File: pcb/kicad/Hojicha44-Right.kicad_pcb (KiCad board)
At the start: 2 copper layers, 150.5 x 114.6 mm, 54 parts

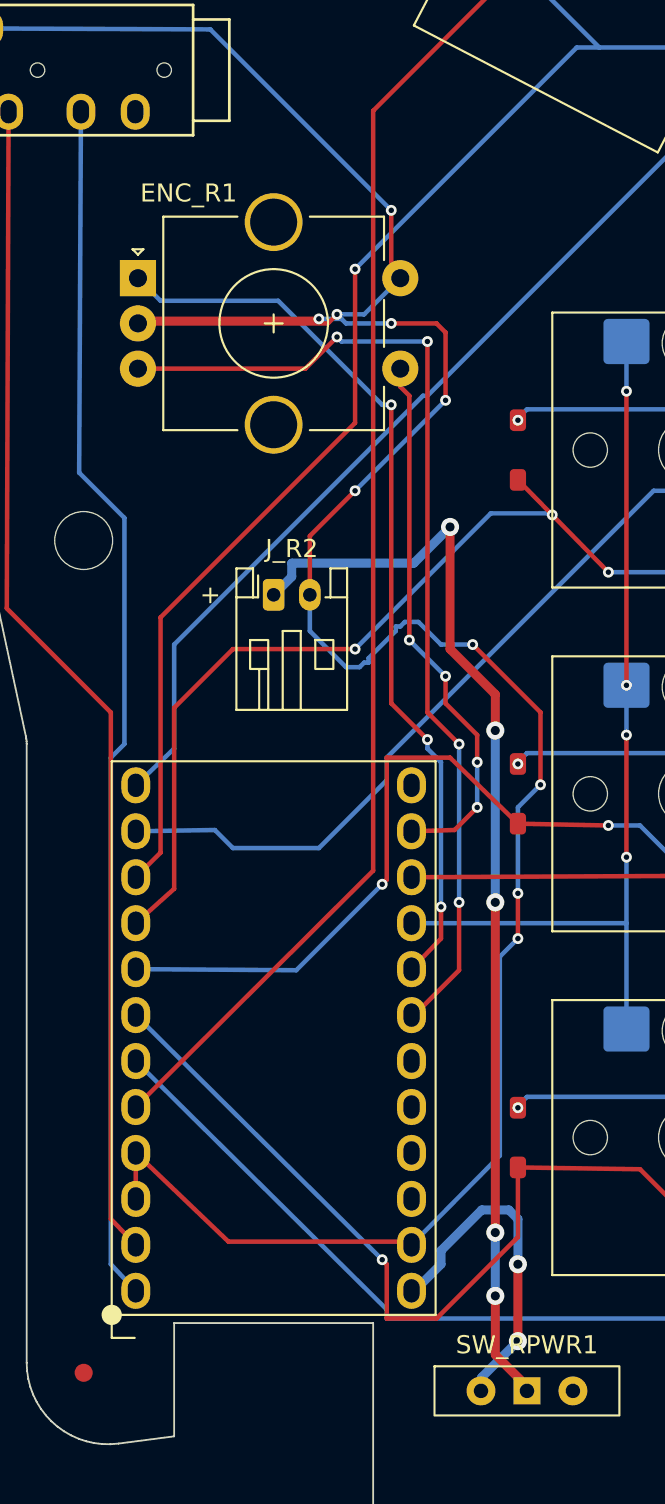
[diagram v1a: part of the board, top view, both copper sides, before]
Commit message: VBAT off USB notch + mask expansion + rating corrections
- Router r13: power-class notch keepout (bite band floor-0.5 to
  floor+2) moves the battery rail off the plug-bump edge; measured
  min VBAT copper-edge to outline 2.518mm both halves (was 0.25mm
  at the notch floor with a via at (111.75,47.5) — both gone).
- Carve/re-block: other-net clearance re-blocked after own carve so
  shared THT slivers steer exits instead of grazing (fixed the
  GND-vs-COL2 graze the reroute exposed). DRC green both halves.
- Mask expansion 0.05 (was 0) in both .kicad_pro; no reroute needed.
- WS-SLTV corrected to 300mA switching; boost jumper stays OPEN;
  100x100 pricing note; USB-cable dry-fit note in first-article.
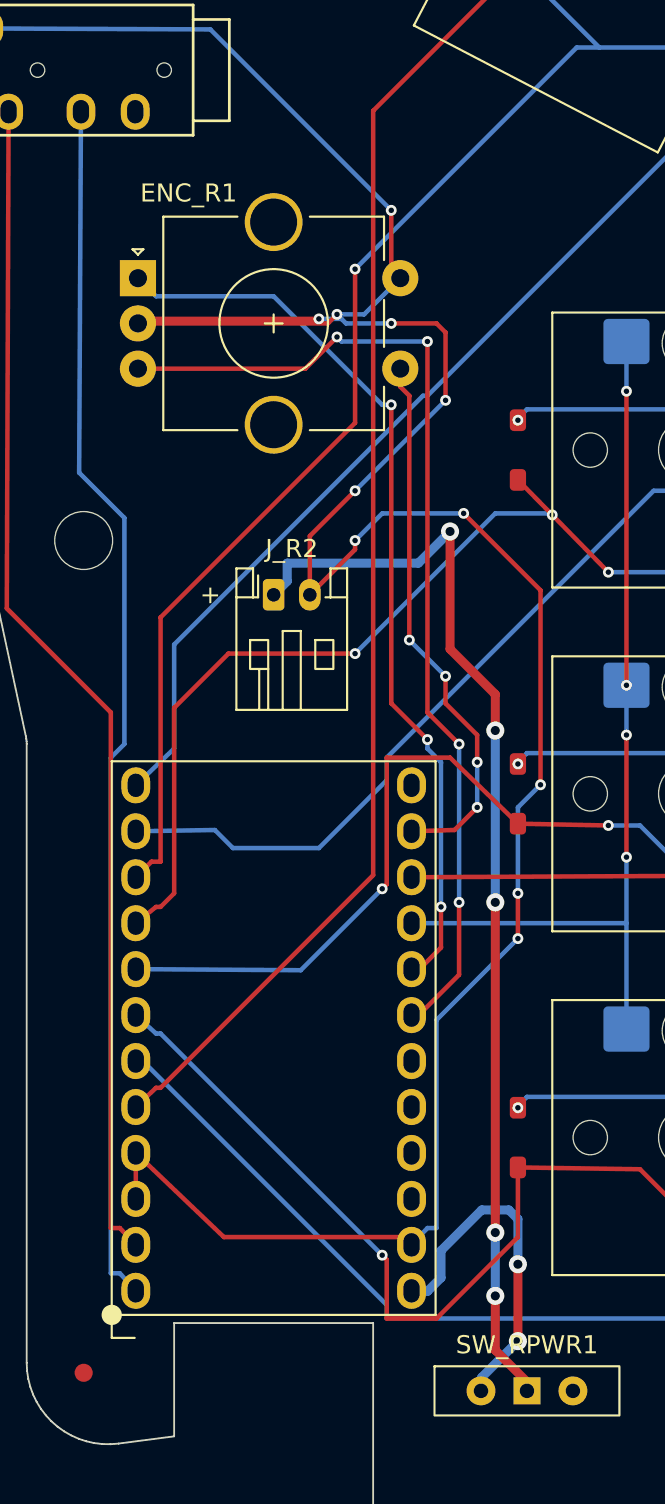
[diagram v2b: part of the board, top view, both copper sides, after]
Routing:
- net GND: track 152.0 -> 156.8 mm, vias 10 -> 11

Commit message: Review F1-F8: diode cathode ticks, doc reconciliation
- F1: generator-owned F.SilkS cathode tick on all 44 SOD-123s (0.29mm
  local clearance, rotation-proof); DRC 0 new silk violations, audit
  symmetric; on-board polarity gate now met
- F8: gpio-map.md right-half tip/ring1 wording fixed (nets were correct)
- F2/F3/F5/F6: no-pour decision, KiCad CPL convention, boot-width and
  TRRS-22.40 lines in first-article; 13.5 rebuttal with footprint math
- 13.5 mouth-gap claim rebutted (no geometric basis; 22.40 stands)
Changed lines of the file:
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@@
 		)
 	)
+	(fp_line (start -2.45 -0.5) (end -2.45 0.5) (stroke (width 0.12) (type solid)) (layer "F.SilkS"))
 )
 (footprint "Hojicha44:SW_Hotswap_Kailh_Choc_V1_1.00u"
@@
 		)
 	)
+	(fp_line (start -2.45 -0.5) (end -2.45 0.5) (stroke (width 0.12) (type solid)) (layer "F.SilkS"))
 )
 (footprint "Hojicha44:SW_Hotswap_Kailh_Choc_V1_1.00u"
@@
 		)
 	)
+	(fp_line (start -2.45 -0.5) (end -2.45 0.5) (stroke (width 0.12) (type solid)) (layer "F.SilkS"))
 )
 (footprint "Hojicha44:SW_Hotswap_Kailh_Choc_V1_1.00u"
@@
 		)
 	)
+	(fp_line (start -2.45 -0.5) (end -2.45 0.5) (stroke (width 0.12) (type solid)) (layer "F.SilkS"))
 )
 (footprint "Hojicha44:SW_Hotswap_Kailh_Choc_V1_1.00u"
@@
 		)
 	)
+	(fp_line (start -2.45 -0.5) (end -2.45 0.5) (stroke (width 0.12) (type solid)) (layer "F.SilkS"))
 )
 (footprint "Hojicha44:SW_Hotswap_Kailh_Choc_V1_1.00u"
@@
 		)
 	)
+	(fp_line (start -2.45 -0.5) (end -2.45 0.5) (stroke (width 0.12) (type solid)) (layer "F.SilkS"))
 )
 (footprint "Hojicha44:SW_Hotswap_Kailh_Choc_V1_1.00u"
@@
 		)
 	)
+	(fp_line (start -2.45 -0.5) (end -2.45 0.5) (stroke (width 0.12) (type solid)) (layer "F.SilkS"))
 )
 (footprint "Hojicha44:SW_Hotswap_Kailh_Choc_V1_1.00u"
@@
 		)
 	)
+	(fp_line (start -2.45 -0.5) (end -2.45 0.5) (stroke (width 0.12) (type solid)) (layer "F.SilkS"))
 )
 (footprint "Hojicha44:SW_Hotswap_Kailh_Choc_V1_1.00u"
@@
 		)
 	)
+	(fp_line (start -2.45 -0.5) (end -2.45 0.5) (stroke (width 0.12) (type solid)) (layer "F.SilkS"))
 )
 (footprint "Hojicha44:SW_Hotswap_Kailh_Choc_V1_1.00u"
@@
 		)
 	)
+	(fp_line (start -2.45 -0.5) (end -2.45 0.5) (stroke (width 0.12) (type solid)) (layer "F.SilkS"))
 )
 (footprint "Hojicha44:SW_Hotswap_Kailh_Choc_V1_1.00u"
@@
 		)
 	)
+	(fp_line (start -2.45 -0.5) (end -2.45 0.5) (stroke (width 0.12) (type solid)) (layer "F.SilkS"))
 )
 (footprint "Hojicha44:SW_Hotswap_Kailh_Choc_V1_1.00u"
@@
 		)
 	)
+	(fp_line (start -2.45 -0.5) (end -2.45 0.5) (stroke (width 0.12) (type solid)) (layer "F.SilkS"))
 )
 (footprint "Hojicha44:SW_Hotswap_Kailh_Choc_V1_1.00u"
@@
 		)
 	)
+	(fp_line (start -2.45 -0.5) (end -2.45 0.5) (stroke (width 0.12) (type solid)) (layer "F.SilkS"))
 )
 (footprint "Hojicha44:SW_Hotswap_Kailh_Choc_V1_1.00u"
@@
 		)
 	)
+	(fp_line (start -2.45 -0.5) (end -2.45 0.5) (stroke (width 0.12) (type solid)) (layer "F.SilkS"))
 )
 (footprint "Hojicha44:SW_Hotswap_Kailh_Choc_V1_1.00u"
@@
 		)
 	)
+	(fp_line (start -2.45 -0.5) (end -2.45 0.5) (stroke (width 0.12) (type solid)) (layer "F.SilkS"))
 )
 (footprint "Hojicha44:SW_Hotswap_Kailh_Choc_V1_1.00u"
@@
 		)
 	)
+	(fp_line (start -2.45 -0.5) (end -2.45 0.5) (stroke (width 0.12) (type solid)) (layer "F.SilkS"))
 )
 (footprint "Hojicha44:SW_Hotswap_Kailh_Choc_V1_1.00u"
@@
 		)
 	)
+	(fp_line (start -2.45 -0.5) (end -2.45 0.5) (stroke (width 0.12) (type solid)) (layer "F.SilkS"))
 )
 (footprint "Hojicha44:SW_Hotswap_Kailh_Choc_V1_1.00u"
@@
 		)
 	)
+	(fp_line (start -2.45 -0.5) (end -2.45 0.5) (stroke (width 0.12) (type solid)) (layer "F.SilkS"))
 )
 (footprint "Hojicha44:SW_Hotswap_Kailh_Choc_V1_1.00u"
@@
 		)
 	)
+	(fp_line (start -2.45 -0.5) (end -2.45 0.5) (stroke (width 0.12) (type solid)) (layer "F.SilkS"))
 )
 (footprint "Hojicha44:SW_Hotswap_Kailh_Choc_V1_1.00u"
@@
 		)
 	)
+	(fp_line (start -2.45 -0.5) (end -2.45 0.5) (stroke (width 0.12) (type solid)) (layer "F.SilkS"))
 )
 (footprint "Hojicha44:SW_Hotswap_Kailh_Choc_V1_1.00u"
@@
 		)
 	)
+	(fp_line (start -2.45 -0.5) (end -2.45 0.5) (stroke (width 0.12) (type solid)) (layer "F.SilkS"))
 )
 (footprint "Hojicha44:SW_Hotswap_Kailh_Choc_V1_1.00u"
@@
 		)
 	)
+	(fp_line (start -2.45 -0.5) (end -2.45 0.5) (stroke (width 0.12) (type solid)) (layer "F.SilkS"))
 )
 (footprint "Hojicha44:Socket_Strips_2x12_P2.54mm_NiceNano"
